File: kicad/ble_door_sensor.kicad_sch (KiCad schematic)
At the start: 42 parts, among them J1 Prog Header, J2 Prog Header, P10 TestPoint, P12 TestPoint, P14 TestPoint, P19 TestPoint, P20 TestPoint, P27 TestPoint, P29 TestPoint, P3 TestPoint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

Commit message: Updated schematic
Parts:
- removed C10, C12: C_Small, Capacitor_SMD:C_0402_1005Metric, symbol Device:C_Small
- removed C14: 100nF, Capacitor_SMD:C_0603_1608Metric, symbol Device:C
- removed DCC1: TestPoint, TestPoint:TestPoint_Pad_D1.5mm, symbol Connector:TestPoint
- removed L2: L, Inductor_SMD:L_0402_1005Metric, symbol Device:L
- removed R3: 0R, Resistor_SMD:R_0603_1608Metric, symbol Device:R
- removed R4: 470k, Resistor_SMD:R_0603_1608Metric, symbol Device:R
- removed U2, U3: A3214ELHLT-T, Package_TO_SOT_SMD:SOT-23W, symbol Sensor_Magnetic:A3214ELHLT-T
- added C101, C102, C103, C104: 100nF, Capacitor_SMD:C_0603_1608Metric, symbol Device:C
- added D101: LED, LED_SMD:LED_0603_1608Metric, symbol Device:LED
- added H101, H102: MountingHole, symbol Mechanical:MountingHole
- added J101: Conn_01x03_Pin, Connector_PinHeader_2.54mm:PinHeader_1x03_P2.54mm_Vertical_SMD_Pin1Left, symbol Connector:Conn_01x03_Pin
- added L101: 15nH, Inductor_SMD:L_0402_1005Metric, symbol Device:L
- added L102: 10uH, Inductor_SMD:L_0603_1608Metric, symbol Device:L
- added R101: 100k, Resistor_SMD:R_0603_1608Metric, symbol Device:R
- added R102: 1K, Resistor_SMD:R_0603_1608Metric, symbol Device:R
- added R103, R104, R105: 470k, Resistor_SMD:R_0603_1608Metric, symbol Device:R
- added SW101: SW_Reed, Library:reed_contact, symbol Switch:SW_Reed
- added SW102: SW_Push, Button_Switch_SMD:SW_SPST_TL3342, symbol Switch:SW_Push
- added SW103, SW104, SW105, SW106: REED_EXT, Connector_PinHeader_1.00mm:PinHeader_1x02_P1.00mm_Vertical, symbol Switch:SW_Reed
- L1: value 3.3nF -> 3.3nH
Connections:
- net GND: now also C101.2, C102.2, C103.2, C104.2, D101.1 (K), J101.3 (Pin_3), SW101.1, SW102.1, SW103.1, SW104.1, SW105.1, SW106.1
- net ONBOARD_HALL: now also C13.1, R2.2, U1.14 (P0.11), SW101.2, SW106.2; no longer U1.19 (P0.16)
- net VCC: now also R101.1, R103.1, R104.1, R105.1
- net at L1.2: now also AE1.1 (A)
- net at U1.47 (DCC): now also L101.2
- net at C5.1, U1.46 (DEC4): now also L102.1
- net ONBOARD_HALL_2: no longer names the net of U1.6 (P0.04/AIN2)
- new net: L101.1, L102.2
- new net: D101.2 (A), R102.2
- new net BUTTON: C101.1, R101.2, SW102.2
- new net EXT_HALL_1: C102.1, R103.2, SW103.2
- new net EXT_HALL_2: C103.1, R104.2, SW104.2
- new net EXT_HALL_3: C104.1, R105.2, SW105.2
- new net LED: R102.1
- new net RX: J101.1 (Pin_1)
- new net TX: J101.2 (Pin_2)
- no-connect marks 17 -> 18
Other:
- moved on the sheet: BT1, C13, C4, L1, R2, TP1, TP2

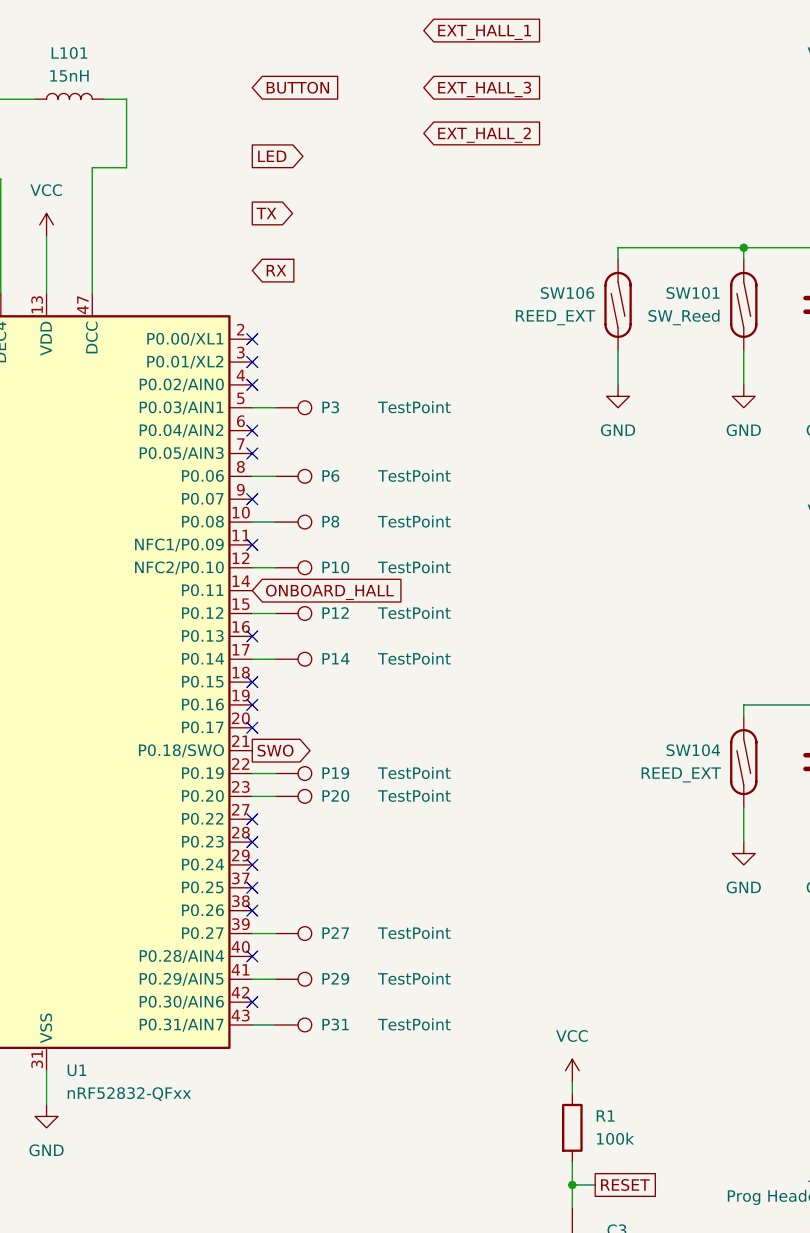
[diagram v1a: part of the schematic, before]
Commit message: First rough placement
Updated some footprints in the process to better fit my needs

Holes are in 5mm grid to each other 15mm in x and 45 mm in y apart

Board outline is 20x80mm
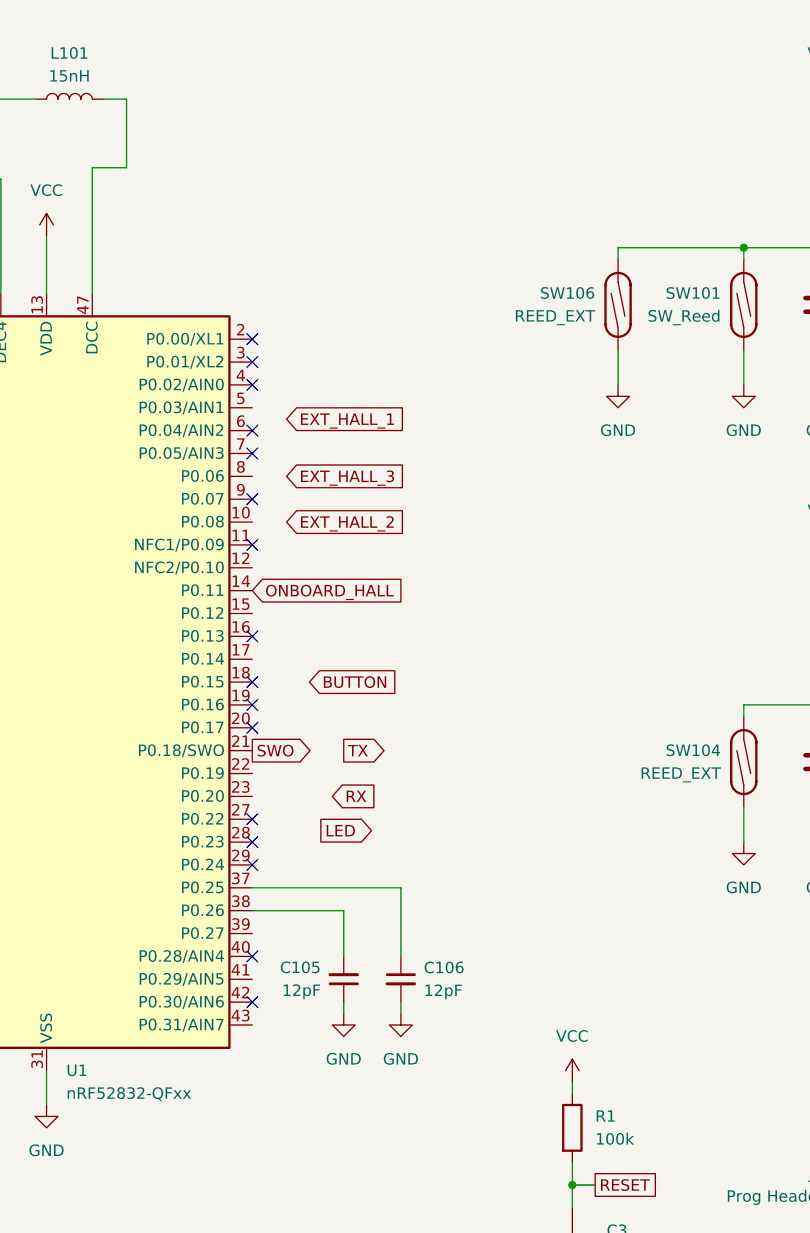
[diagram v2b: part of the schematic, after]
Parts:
- removed P10, P12, P14, P19, P20, P27, P29, P3, P31, P6, P8: TestPoint, TestPoint:TestPoint_Pad_D1.5mm, symbol Connector:TestPoint
- added C105, C106: 12pF, Capacitor_SMD:C_0402_1005Metric, symbol Device:C_Small
- C1, C101, C102, C103, C104, C11, C13, C3: footprint Capacitor_SMD:C_0603_1608Metric -> Capacitor_SMD:C_0402_1005Metric; LCSC# C14663 -> C1525
- H101, H102: footprint (none) -> MountingHole:MountingHole_2.2mm_M2
- R1, R101: footprint Resistor_SMD:R_0603_1608Metric -> Resistor_SMD:R_0402_1005Metric; LCSC# C25803 -> C25741
- R102: LCSC# (none) -> C21190
- R103, R104, R105, R2: footprint Resistor_SMD:R_0603_1608Metric -> Resistor_SMD:R_0402_1005Metric; LCSC# C23178 -> C25790
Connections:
- net GND: now also C105.1, C106.2
- net at U1.37 (P0.25): now also C106.1
- net at U1.38 (P0.26): now also C105.2
- no-connect marks 18 -> 16

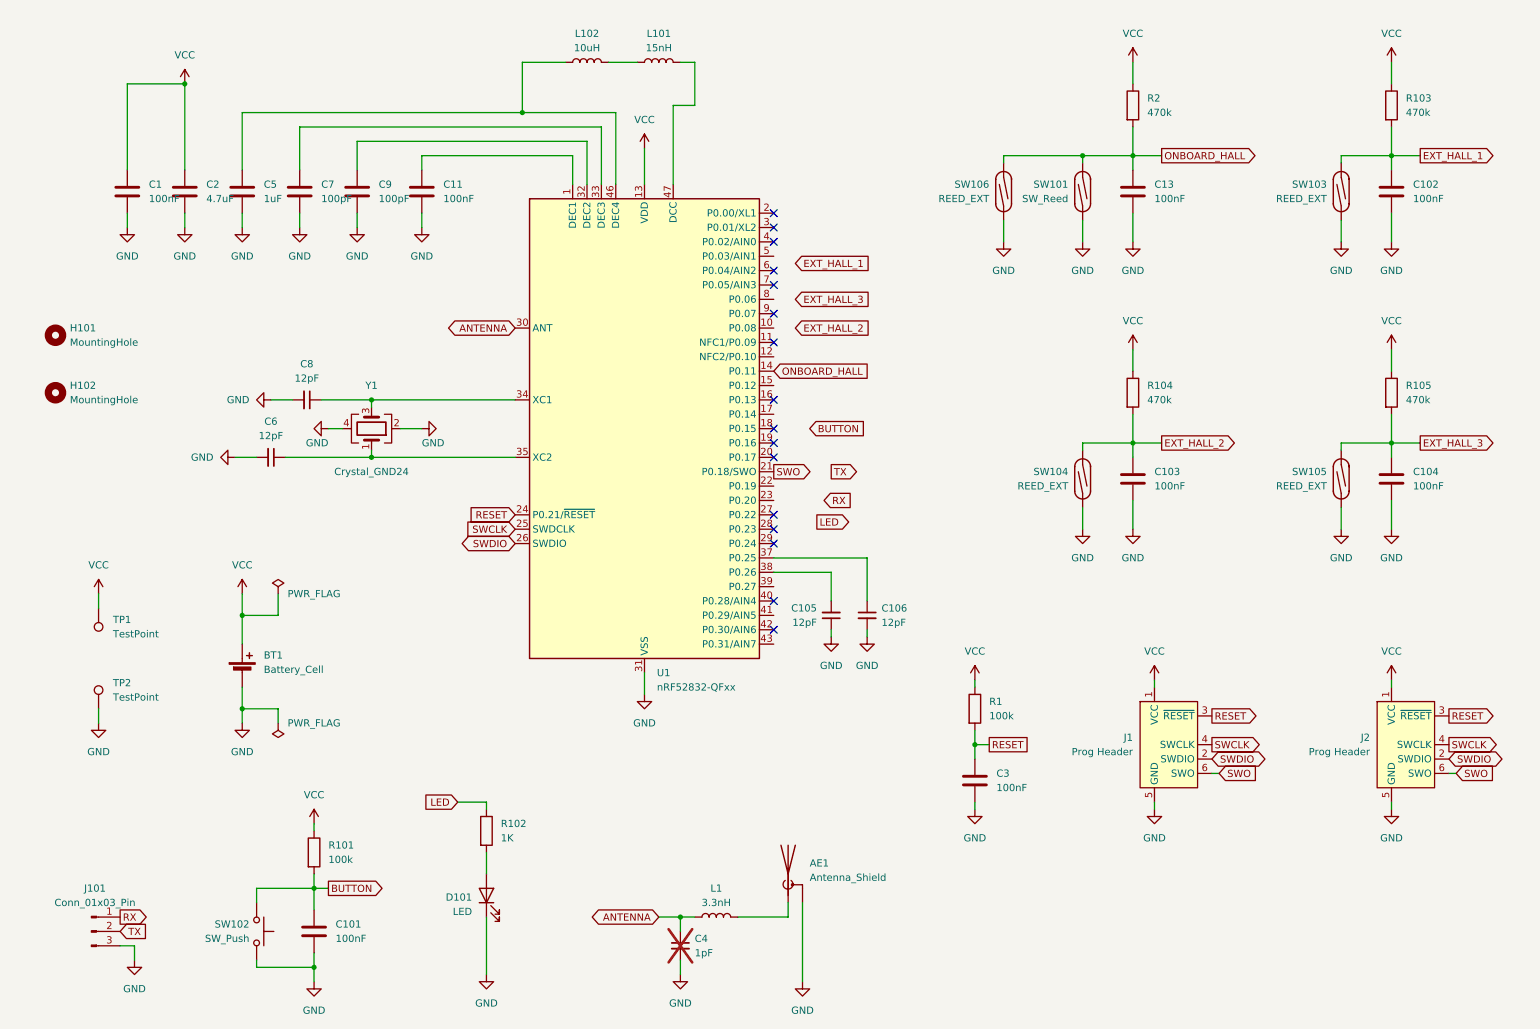
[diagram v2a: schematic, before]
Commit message: First routing
Replaced Testpoints with SMD pinheader
Added more Testpoints
Reduced board outline to 20x70mm
Mounting holes are now 15x35mm apart
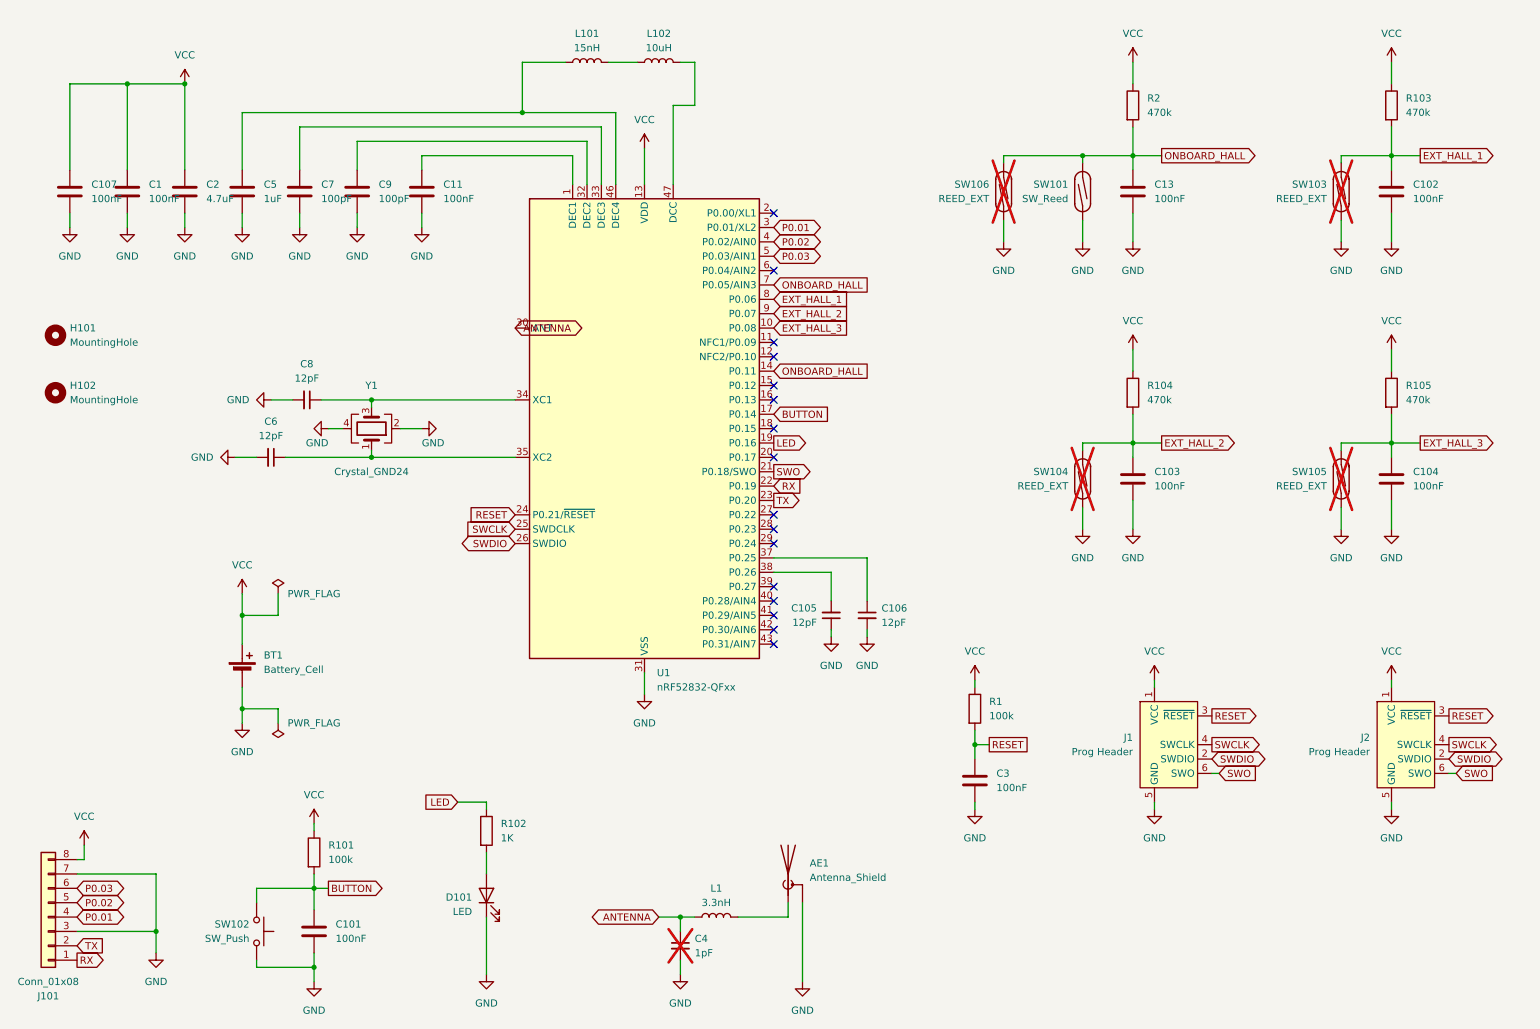
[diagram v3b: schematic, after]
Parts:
- removed J101: Conn_01x03_Pin, Connector_PinHeader_2.54mm:PinHeader_1x03_P2.54mm_Vertical_SMD_Pin1Left, symbol Connector:Conn_01x03_Pin
- removed TP1, TP2: TestPoint, TestPoint:TestPoint_Pad_3.0x3.0mm, symbol Connector:TestPoint
- added C107: 100nF, Capacitor_SMD:C_0402_1005Metric, symbol Device:C
- added J101: Conn_01x08, Connector_PinHeader_2.54mm:PinHeader_1x08_P2.54mm_Vertical_SMD_Pin1Left, symbol Connector_Generic:Conn_01x08
- D101: LCSC# (none) -> C72043
- H101, H102: LCSC# (none) -> -; now left out of the parts list
- SW101: LCSC# (none) -> -
- SW103, SW104, SW105, SW106: LCSC# (none) -> -; now not fitted
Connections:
- net BUTTON: now also U1.17 (P0.14)
- net EXT_HALL_1: now also U1.8 (P0.06)
- net EXT_HALL_2: now also U1.9 (P0.07)
- net EXT_HALL_3: now also U1.10 (P0.08)
- net GND: now also C107.2, J101.3 (Pin_3), J101.7 (Pin_7)
- net LED: now also U1.19 (P0.16)
- net ONBOARD_HALL: now also U1.7 (P0.05/AIN3)
- net RX: now also U1.22 (P0.19), J101.1 (Pin_1)
- net TX: now also U1.23 (P0.20), J101.2 (Pin_2)
- net VCC: now also C107.1, J101.8 (Pin_8)
- net at C5.1, U1.46 (DEC4): now also L101.1; no longer L102.1
- net at L102.2: now also U1.47 (DCC); no longer L101.1
- net P0.01: now reaches U1.3 (P0.01/XL2)
- net P0.01: now also J101.4 (Pin_4)
- net P0.02: now reaches U1.4 (P0.02/AIN0)
- net P0.02: now also J101.5 (Pin_5)
- net at L101.2: now also L102.1; no longer U1.47 (DCC)
- net P0.03: now reaches U1.5 (P0.03/AIN1)
- net P0.03: now also J101.6 (Pin_6)
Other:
- moved on the sheet: L101, L102

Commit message: Put the reed contact on the top side
I want to glue the PCB to some surfaces and having something on the
bottom side is very contraproductive.
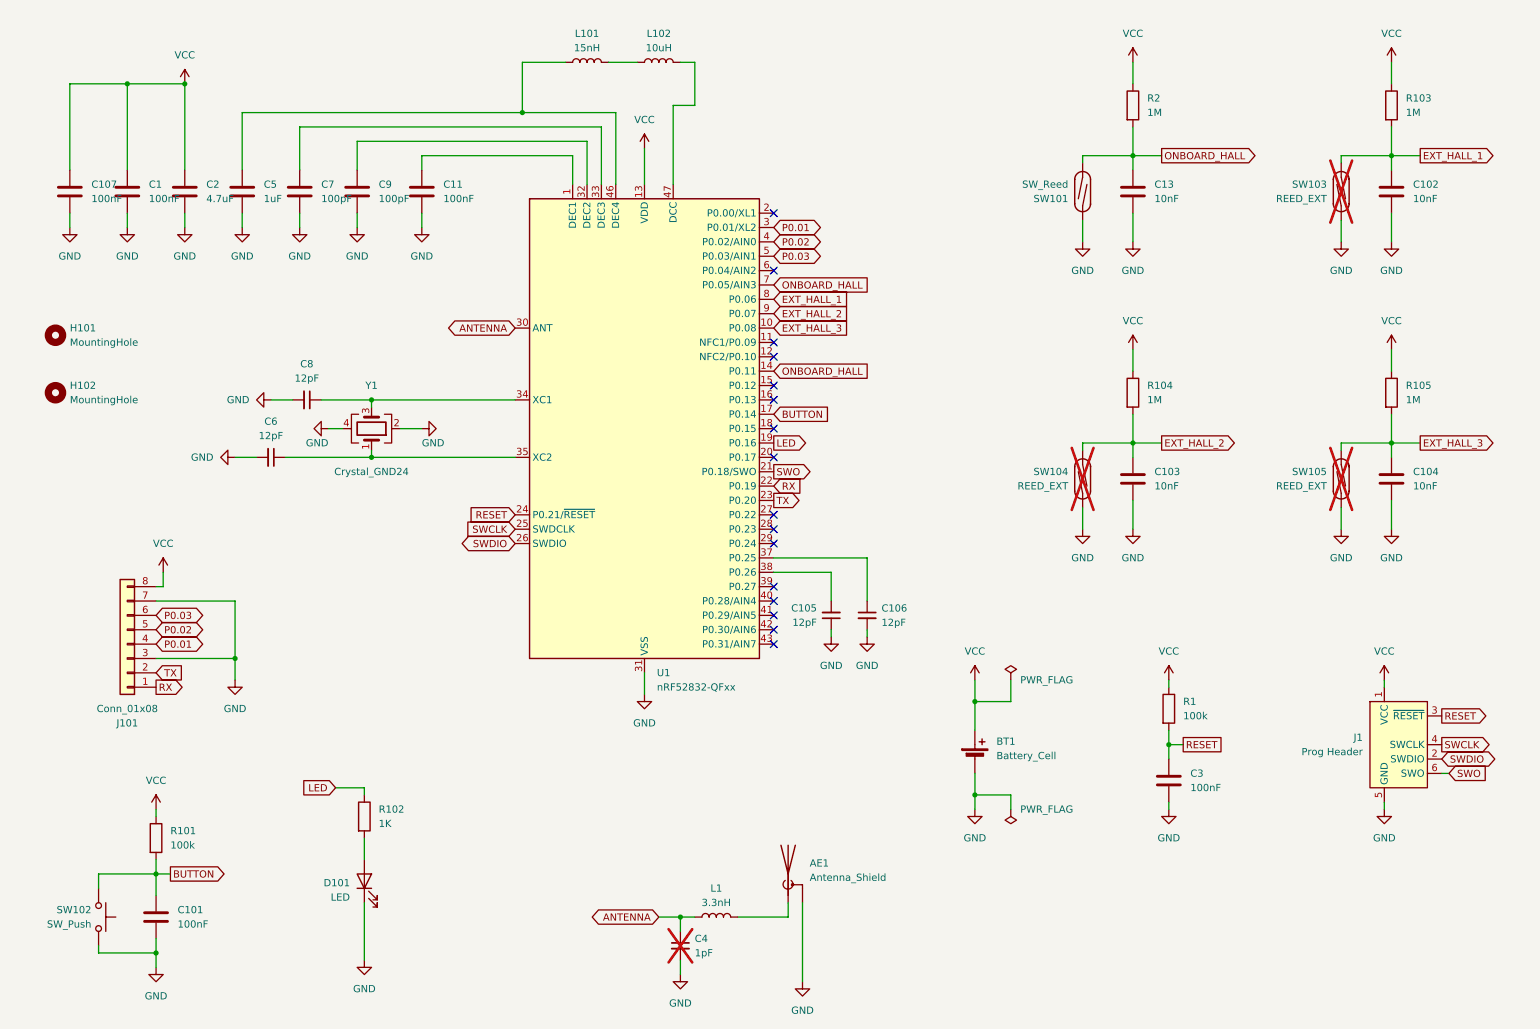
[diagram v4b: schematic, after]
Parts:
- removed J2: Prog Header, Connector:Tag-Connect_TC2030-IDC-NL_2x03_P1.27mm_Vertical, symbol Connector:Conn_ARM_SWD_TagConnect_TC2030-NL
- removed SW106: REED_EXT, Connector_PinHeader_1.00mm:PinHeader_1x02_P1.00mm_Vertical, symbol Switch:SW_Reed
- C102, C103, C104, C13: value 100nF -> 10nF; LCSC# C1525 -> C15195
- R103, R104, R105, R2: value 470k -> 1M; LCSC# C25790 -> C26083
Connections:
- net GND: now also SW101.2; no longer SW101.1
- net ONBOARD_HALL: now also SW101.1; no longer SW101.2
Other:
- moved on the sheet: BT1, C101, C3, D101, J1, J101, R1, R101, R102, SW102
